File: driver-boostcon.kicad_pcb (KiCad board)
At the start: 2 copper layers, 58 parts, among them J301 Fuse Bypass, P301 On Switch, P302 Vcc, P303 PowerGND, P304 RegulatedPWR, P601 Programmer, Q401 IRF4905S, Q402 BSC016N04LS, SW601 SW_Push, U601 ATMEGA328P-PU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

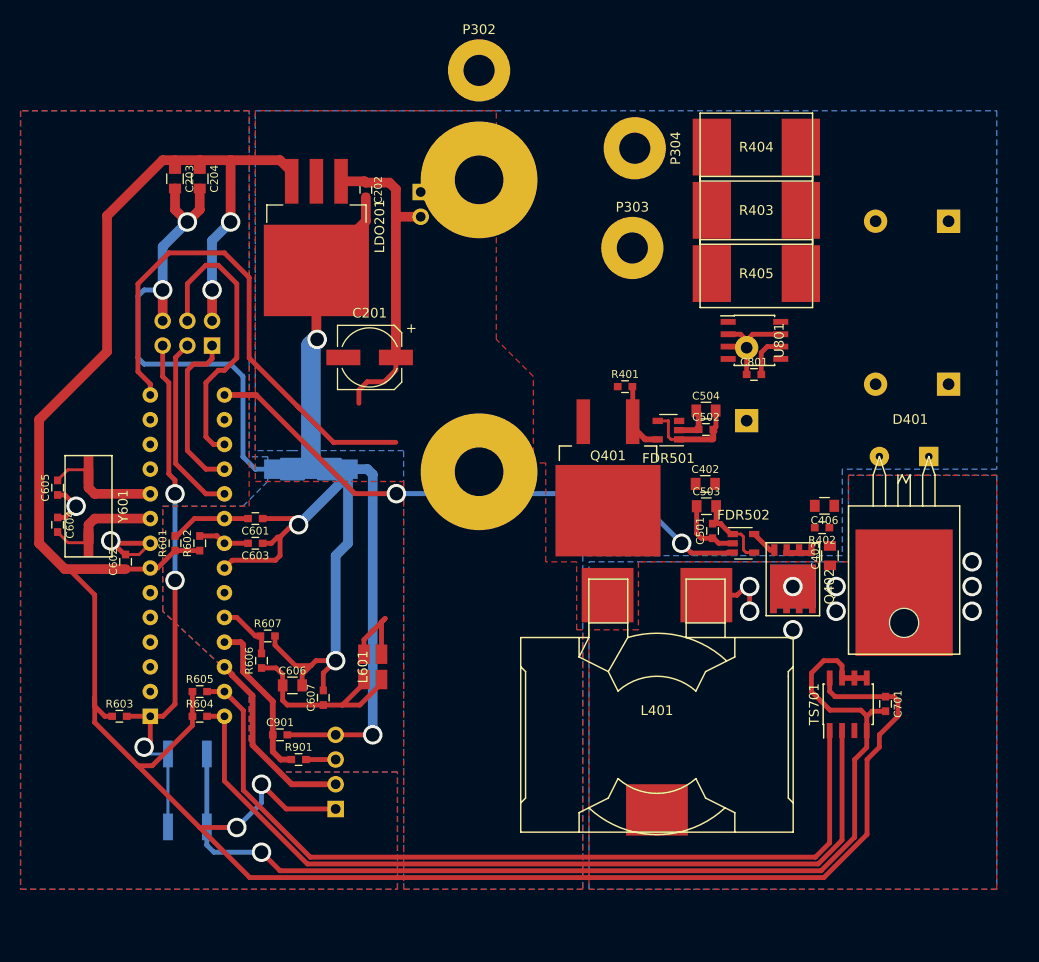
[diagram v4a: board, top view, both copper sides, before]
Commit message: Reworked layout and added heatsink.
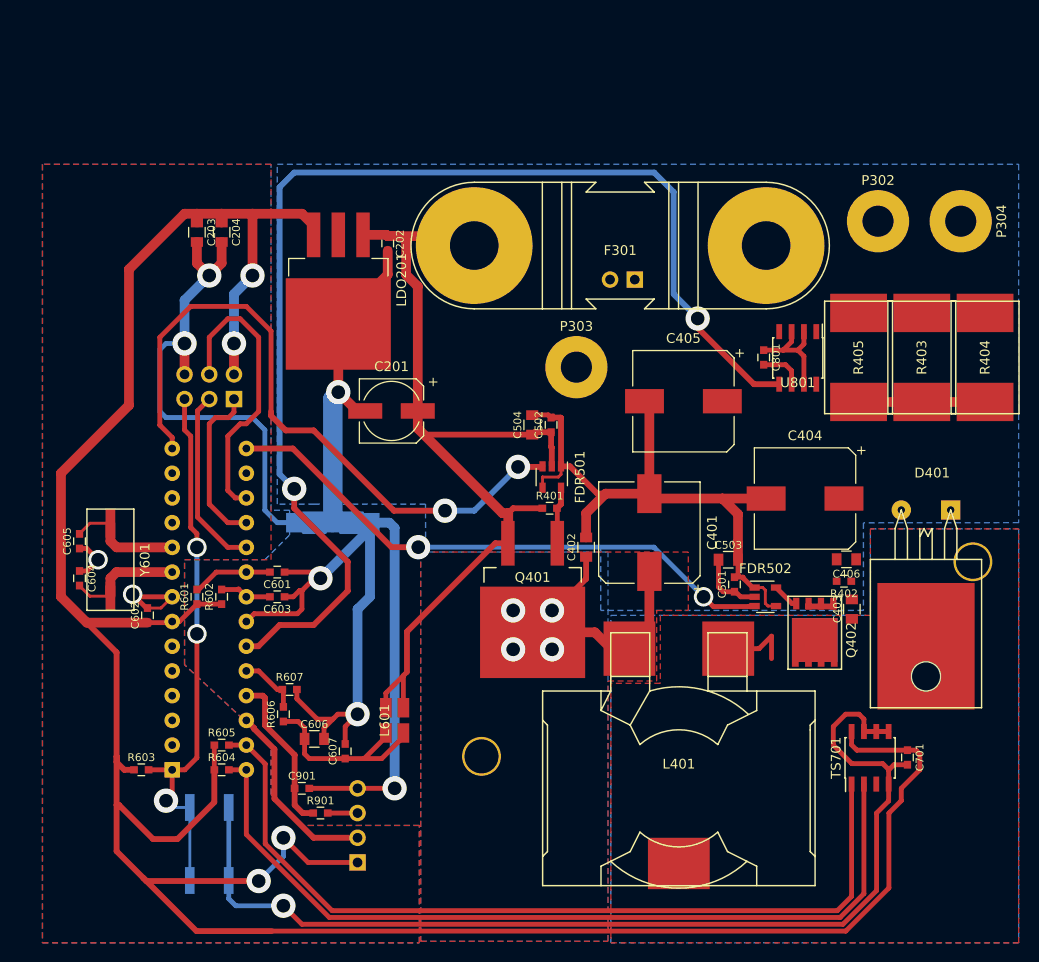
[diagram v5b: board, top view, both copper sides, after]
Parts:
- added REF**: Heatsink_73.5x49, axel:Heatsink_73.5x49, B.Cu at (150.0, 93.5)
- C401: value 2200 uF -> 470 uF; footprint Capacitors_ThroughHole:CP_Radial_D16.0mm_P7.50mm -> Capacitors_SMD:CP_Elec_10x10.5; moved to F.Cu
- C404, C405: value 1000 uF -> 470 uF; footprint Capacitors_ThroughHole:CP_Radial_D16.0mm_P7.50mm -> Capacitors_SMD:CP_Elec_10x10.5; moved to F.Cu
- F301: moved to F.Cu
- moved P302 43.8 mm to (135.8, 68.5)
- moved P304 34.3 mm to (144.2, 68.5)
- moved C405 32.9 mm to (115.8, 87.0)
- moved R404 31.9 mm to (146.8, 82.5), turned to 90 degrees
- moved J301 23.8 mm to (110.8, 74.5), turned to 90 degrees
- moved R403 22.8 mm to (140.2, 82.5), turned to 90 degrees
- moved C404 18.9 mm to (128.2, 97.0)
- moved C504 17.9 mm to (100.2, 89.4), turned to 90 degrees
- moved F301 16.7 mm to (109.2, 71.0), turned to 0 degrees
- moved C502 15.9 mm to (102.2, 89.4), turned to 90 degrees
- moved C401 15.2 mm to (112.2, 100.5)
- moved Q401 14.7 mm to (100.2, 106.2)
- moved R401 14.7 mm to (102.0, 98.0)
- moved C402 13.9 mm to (105.8, 102.0), turned to 90 degrees
- moved R405 13.6 mm to (133.8, 82.5), turned to 90 degrees
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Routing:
- net /CurrentSense/CurrentSignal: track 0.00 -> 124.9 mm, vias 0 -> 2
- net VCC: track 52.8 -> 104.8 mm
- net GNDPWR: track 57.6 -> 107.8 mm
- net /Power stage/PowerVcc: track 0.00 -> 29.5 mm, vias 0 -> 4
- net +5C: track 262.3 -> 282.9 mm
- net /MCU/PowerDriveSignal: track 53.1 -> 68.3 mm, vias 0 -> 2
- net /CurrentSense/CurrentSignal+: track 0.00 -> 13.0 mm
- net /MosFET driver/PowerDriveSignal: track 7.28 -> 6.46 mm
- net /Power stage/SwitchNode: vias 3 -> 0
- net (no net): vias 6 -> 0
- added copper zone on B.Cu, net /Power stage/PowerVcc
- added copper zone on F.Cu, net /Power stage/PowerVcc
- removed copper zone on F.Cu, net GNDPWR

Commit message: Added power traces and corrected diode polarity
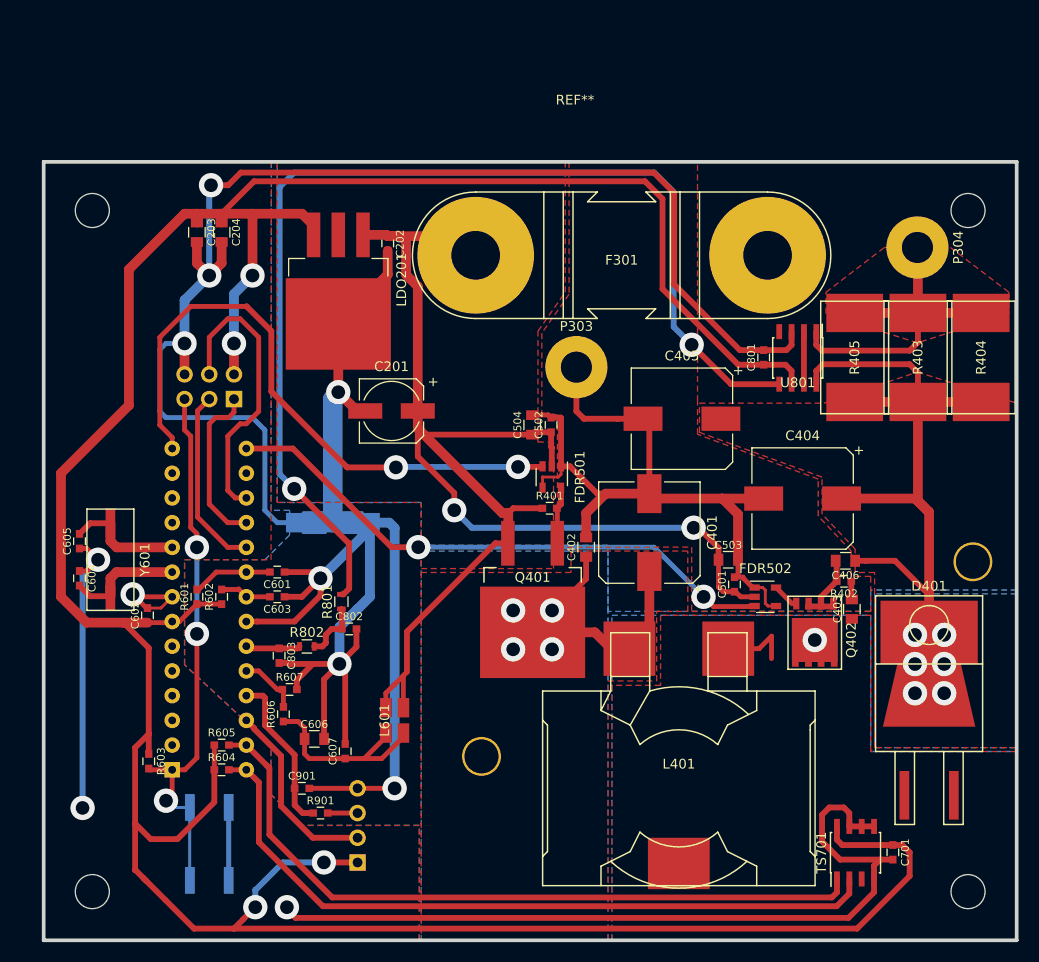
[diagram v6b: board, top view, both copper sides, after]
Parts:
- removed J301: Fuse Bypass, Pin_Headers:Pin_Header_Angled_1x02_Pitch2.54mm
- removed P302: Vcc, Mounting_Holes:MountingHole_3.2mm_M3_Pad
- added C802: 680 nF, axel:C_0603_CustomText, F.Cu at (81.4, 110.4)
- added C803: 680 nF, axel:C_0603_CustomText, F.Cu at (74.2, 113.2)
- added R801: 6k, axel:R_0603_CustomText, F.Cu at (80.6, 107.6)
- added R802: 6k, axel:R_0603_CustomText, F.Cu at (77.0, 112.2)
- added REF**: EuroBoard_halb_Type-I_100mmX80mm_holes, EuroBoard_Outline:EuroBoard_halb_Type-I_100mmX80mm_holes, F.Cu at (50.0, 142.4)
- D401: footprint axel:TO-220AB -> axel:TO220AB-SMD
- moved D401 24.8 mm to (141.0, 123.0), turned to 0 degrees
- moved C701 9.86 mm to (137.3, 133.4)
- moved TS701 9.86 mm to (133.4, 133.4)
- moved P304 5.21 mm to (139.8, 71.2)
- moved C405 1.81 mm to (115.6, 88.8)
- moved R603 1.17 mm to (60.8, 124.0), turned to 270 degrees
- moved F301 1.01 mm to (109.4, 72.0)
- moved R403 0.40 mm to (139.8, 82.5)
- moved R404 0.40 mm to (146.3, 82.5)
- moved R405 0.40 mm to (133.3, 82.5)
- moved C404 0.25 mm to (128.0, 97.0)
- moved C406 0.18 mm to (132.4, 103.4)
- turned C801 to 90 degrees
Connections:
- C801 pad 1: GNDD -> +5C
- C801 pad 2: +5C -> GNDD
- U801 pad 5: /CurrentSense/CurrentSignal -> Net-(R801-Pad2)
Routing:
- net /CurrentSense/CurrentSignal: track 124.9 -> 5.64 mm, vias 2 -> 0
- net Net-(R801-Pad2): track 0.00 -> 114.4 mm, vias 0 -> 2
- net GNDD: track 190.2 -> 275.9 mm, vias 5 -> 7
- net /CurrentSense/CurrentSignal+: track 13.0 -> 75.1 mm, vias 0 -> 6
- net +5C: track 282.9 -> 330.8 mm
- net VCC: track 104.8 -> 144.8 mm, vias 0 -> 2
- net /CurrentSense/CurrentSignal-: track 0.00 -> 35.2 mm
- net GNDPWR: track 107.8 -> 123.2 mm
- net GNDREF: track 96.9 -> 111.4 mm
- net SDA: track 88.9 -> 75.5 mm
- net SCL: track 88.2 -> 75.7 mm
- net Net-(C802-Pad1): track 0.00 -> 6.16 mm
- net /MCU/PowerDriveSignal: track 68.3 -> 63.1 mm
- net Net-(C403-Pad2): track 0.16 -> 2.06 mm
- net /Power stage/SwitchNode: vias 0 -> 1
- added copper zone on B.Cu, net /CurrentSense/CurrentSignal+
- added copper zone on F.Cu, net /CurrentSense/CurrentSignal+
- added copper zone on F.Cu, net /CurrentSense/CurrentSignal-
- added copper zone on F.Cu, net GNDPWR
- added copper zone on F.Cu, net VCC
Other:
- board outline added: 100 x 80 mm
- net class Default: clearance 0.2 -> 0.3
- rule trace_clearance: 0.2 -> 0.3
